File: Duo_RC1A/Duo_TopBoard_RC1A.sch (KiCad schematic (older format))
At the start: 40 parts, among them CN1 CONN_PANNEL_2X2, CN2 CONN_PANNEL_2X2, P1 HEADER_180_2.54_10X2, P2 KK3.96_2, Q1 MMBT3904, Q2 MMBT3904, U4 NCP1117DT33G

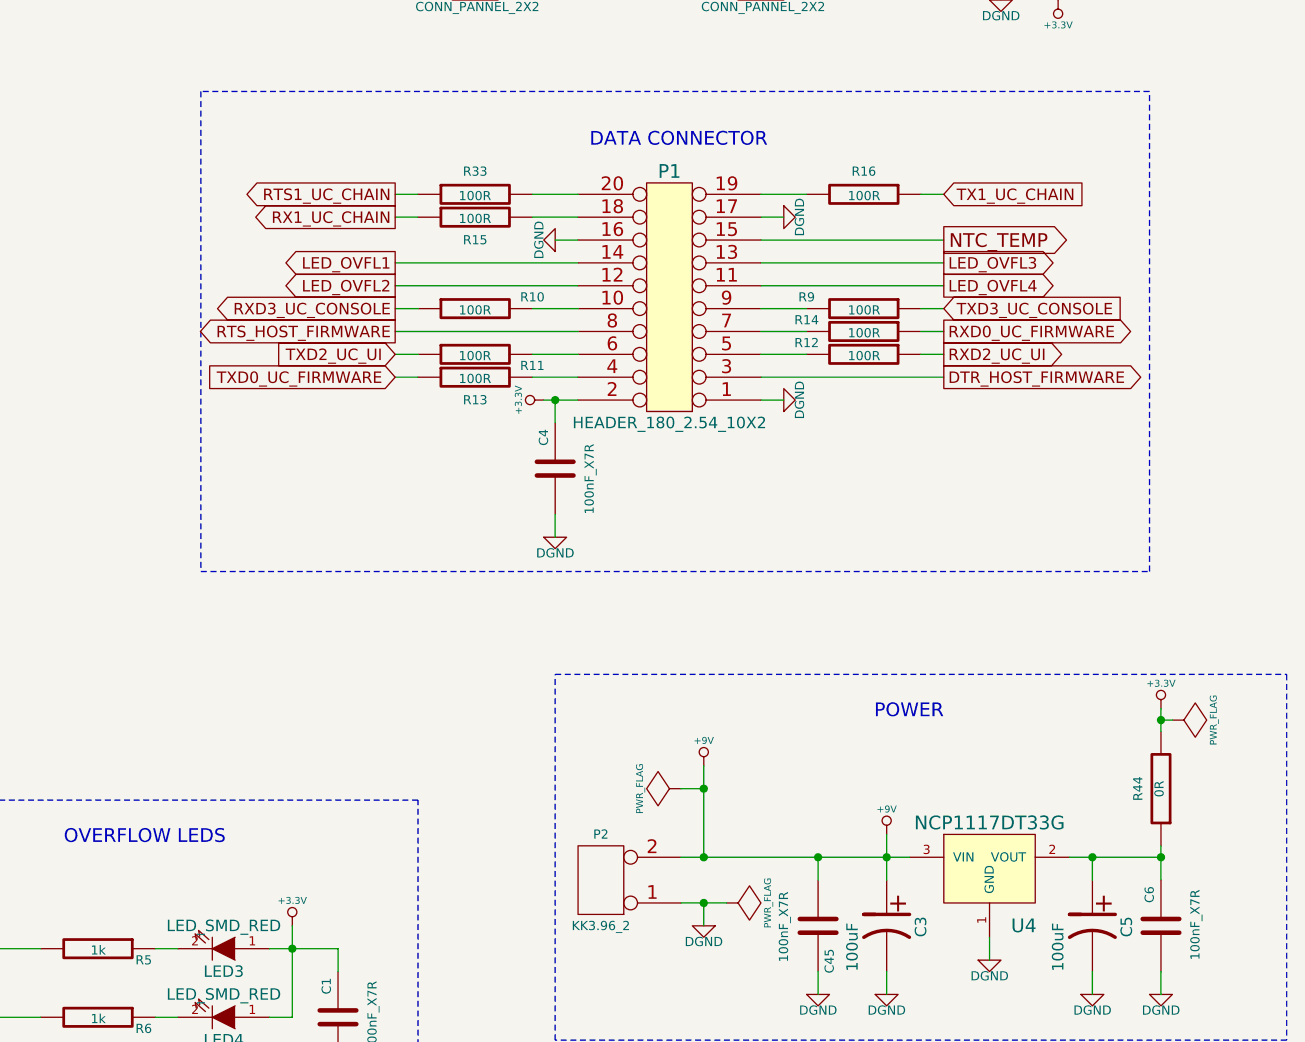
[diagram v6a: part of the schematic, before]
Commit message: Finished the MOD Duo Top Board Schematic and Layout
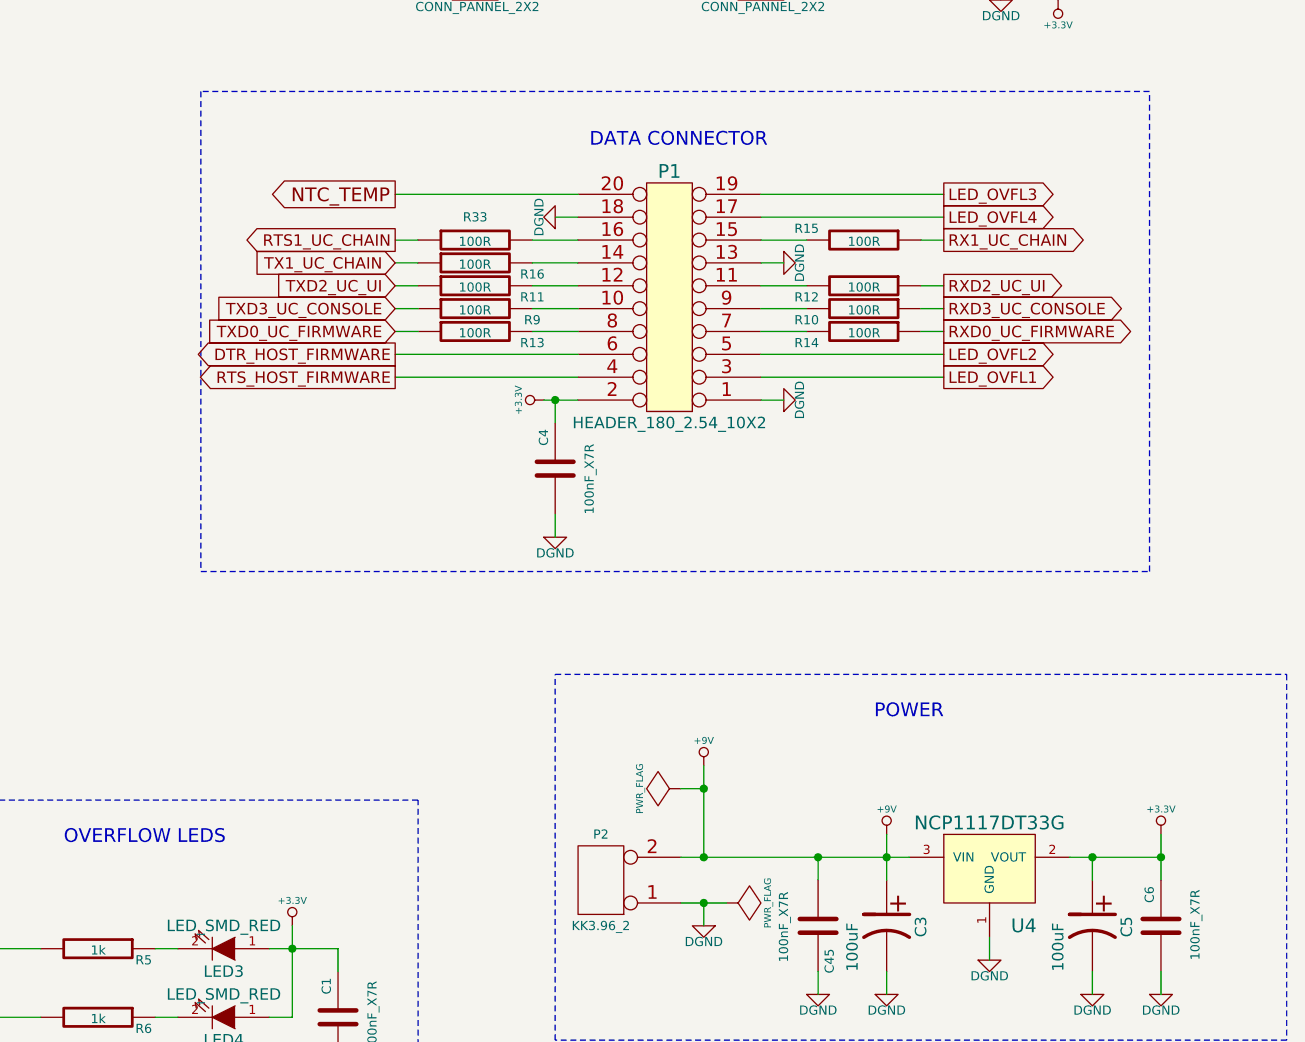
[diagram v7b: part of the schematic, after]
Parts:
- removed R44: 0R, Duo_Audio_HMI_RC1A:SM0805, symbol R
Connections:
- net +3.3V: now also C5.1, C6.1, U4.2 (VOUT)
- net DGND: now also P1.13 (P13), P1.18 (P18); no longer P1.16 (P16), P1.17 (P17)
- net DTR_HOST_FIRMWARE: now also P1.6 (P6); no longer P1.3 (P3)
- net LED_OVFL1: now also P1.3 (P3); no longer P1.14 (P14)
- net LED_OVFL2: now also P1.5 (P5); no longer P1.12 (P12)
- net LED_OVFL3: now also P1.19 (P19); no longer P1.13 (P13)
- net LED_OVFL4: now also P1.17 (P17); no longer P1.11 (P11)
- net NTC_TEMP: now also P1.20 (P20); no longer P1.15 (P15)
- net RTS_HOST_FIRMWARE: now also P1.4 (P4); no longer P1.8 (P8)
- net at R9.2: now also P1.10 (P10); no longer P1.9 (P9)
- net at R10.2: now also P1.9 (P9); no longer P1.10 (P10)
- net at R11.2: now also P1.12 (P12); no longer P1.6 (P6)
- net at R12.2: now also P1.11 (P11); no longer P1.5 (P5)
- net at R13.2: now also P1.8 (P8); no longer P1.4 (P4)
- net at R15.2: now also P1.15 (P15); no longer P1.18 (P18)
- net at R16.2: now also P1.14 (P14); no longer P1.19 (P19)
- net at R33.2: now also P1.16 (P16); no longer P1.20 (P20)
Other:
- moved on the sheet: R10, R11, R12, R13, R15, R16, R33, R9

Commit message: Wrking on the sound. Changed the board size.
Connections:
- net LED_OVFL3: now also P1.20 (P20); no longer P1.19 (P19)
- net LED_OVFL4: now also P1.19 (P19); no longer P1.17 (P17)
- net NTC_TEMP: now also P1.17 (P17); no longer P1.20 (P20)
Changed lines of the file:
@@
 Text GLabel 8900 2850 2    50   Output ~ 0
 LED_OVFL2
+Text GLabel 6500 2150 0    50   Output ~ 0
+LED_OVFL3
 Text GLabel 8900 2150 2    50   Output ~ 0
-LED_OVFL3
-Text GLabel 8900 2250 2    50   Output ~ 0
 LED_OVFL4
 $Comp
@@
 Text GLabel 8900 2350 2    50   Output ~ 0
 RX1_UC_CHAIN
-Text GLabel 6500 2350 0    50   Output ~ 0
+Text GLabel 6500 2350 0    50   Input ~ 0
 RTS1_UC_CHAIN
 $Comp
@@
 	0    -1   1    0
 $EndComp
-Text GLabel 6500 2150 0    60   Output ~ 0
+Text GLabel 8900 2250 2    60   Output ~ 0
 NTC_TEMP
 $Comp
